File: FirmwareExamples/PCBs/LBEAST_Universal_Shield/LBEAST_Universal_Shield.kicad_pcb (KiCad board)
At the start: 2 copper layers, 118 x 84.5 mm, 54 parts, among them J1 MTJ-883X1, J10 CAN BUS, J11 FAN, J2 MTJ-883X1, J3 MTJ-883X1, J4 MTJ-883X1, J5 MTJ-883X1, J6 MTJ-883X1, J7 MTJ-883X1, J8 MTJ-883X1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

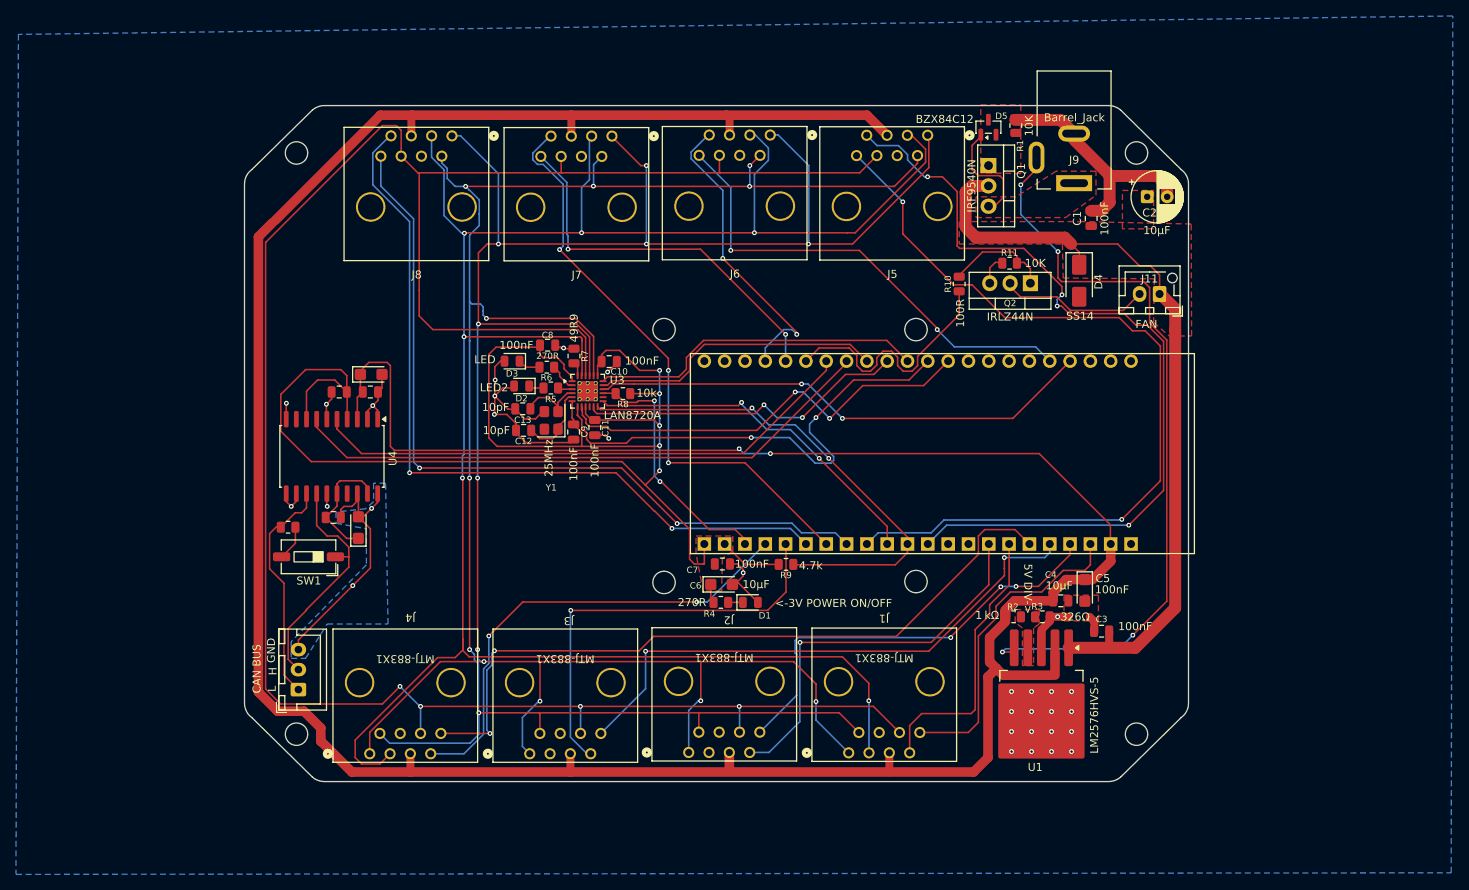
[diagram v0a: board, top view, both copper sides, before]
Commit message: add power differential protection to LBUS aux ports
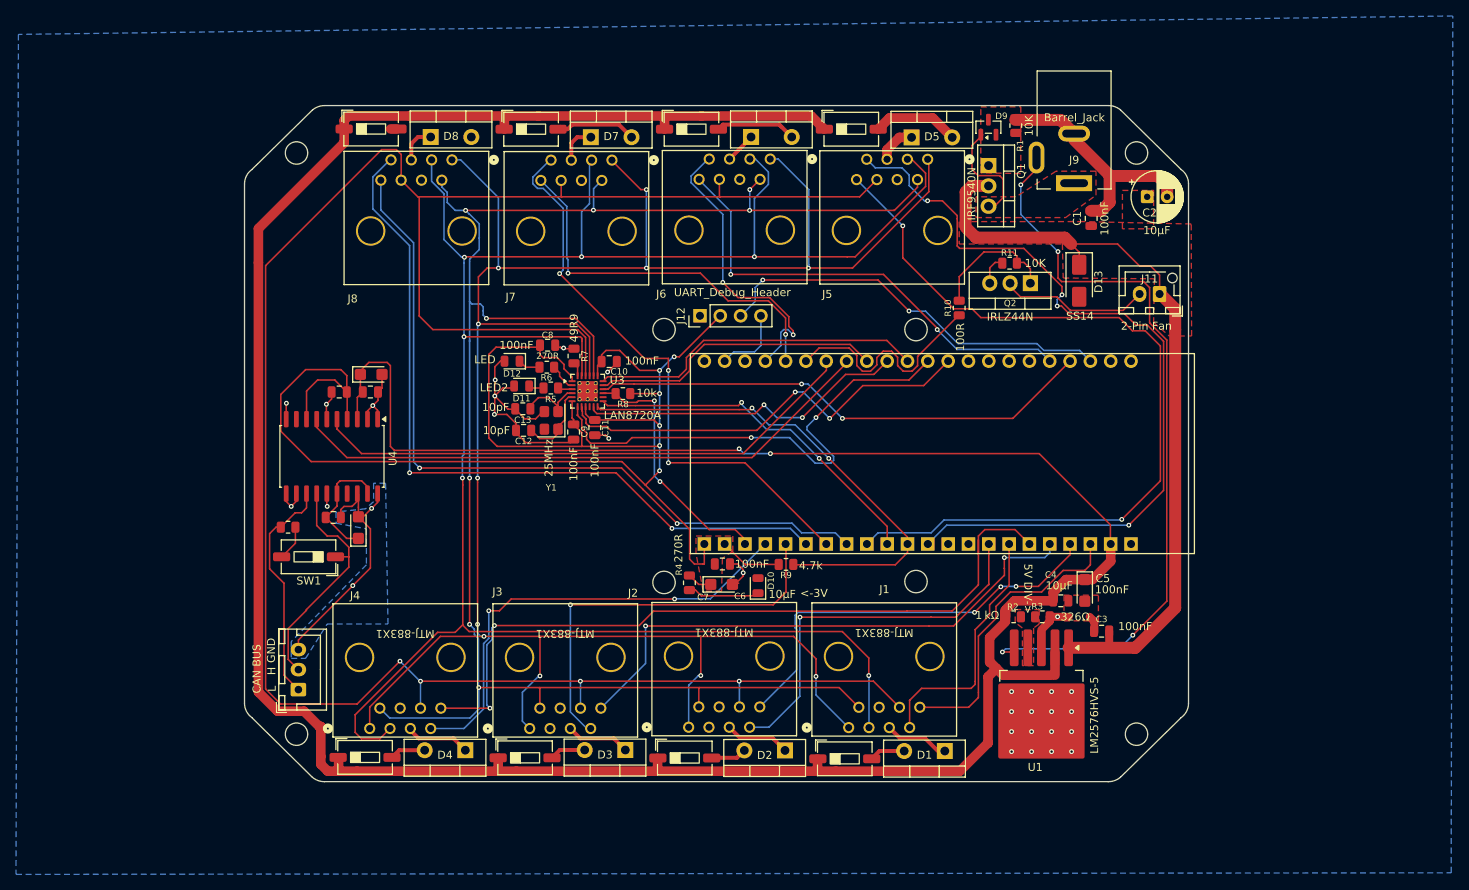
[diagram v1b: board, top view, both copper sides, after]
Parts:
- added D1: MBR735, Package_TO_SOT_THT:TO-220-2_Vertical, F.Cu at (176.1, 135.2)
- added D2: MBR735, Package_TO_SOT_THT:TO-220-2_Vertical, F.Cu at (156.1, 135.1)
- added D3: MBR735, Package_TO_SOT_THT:TO-220-2_Vertical, F.Cu at (136.2, 135.1)
- added D4: MBR735, Package_TO_SOT_THT:TO-220-2_Vertical, F.Cu at (116.2, 135.1)
- added D5: MBR735, Package_TO_SOT_THT:TO-220-2_Vertical, F.Cu at (171.9, 58.5)
- added D6: MBR735, Package_TO_SOT_THT:TO-220-2_Vertical, F.Cu at (151.9, 58.4)
- added D7: MBR735, Package_TO_SOT_THT:TO-220-2_Vertical, F.Cu at (131.9, 58.5)
- added D8: MBR735, Package_TO_SOT_THT:TO-220-2_Vertical, F.Cu at (111.8, 58.4)
- added J12: UART_Debug_Header, Connector_PinHeader_2.54mm:PinHeader_1x04_P2.54mm_Vertical, F.Cu at (145.5, 80.8)
- added SW2: J1_PWR_SW, Button_Switch_SMD:SW_DIP_SPSTx01_Slide_6.7x4.1mm_W6.73mm_P2.54mm_LowProfile_JPin, F.Cu at (163.6, 136.2)
- added SW3: J2_PWR_SW, Button_Switch_SMD:SW_DIP_SPSTx01_Slide_6.7x4.1mm_W6.73mm_P2.54mm_LowProfile_JPin, F.Cu at (143.6, 136.1)
- added SW4: J3_PWR_SW, Button_Switch_SMD:SW_DIP_SPSTx01_Slide_6.7x4.1mm_W6.73mm_P2.54mm_LowProfile_JPin, F.Cu at (123.6, 136.0)
- added SW5: J4_PWR_SW, Button_Switch_SMD:SW_DIP_SPSTx01_Slide_6.7x4.1mm_W6.73mm_P2.54mm_LowProfile_JPin, F.Cu at (103.6, 136.0)
- added SW6: J5_PWR_SW, Button_Switch_SMD:SW_DIP_SPSTx01_Slide_6.7x4.1mm_W6.73mm_P2.54mm_LowProfile_JPin, F.Cu at (164.4, 57.5)
- added SW7: J6_PWR_SW, Button_Switch_SMD:SW_DIP_SPSTx01_Slide_6.7x4.1mm_W6.73mm_P2.54mm_LowProfile_JPin, F.Cu at (144.4, 57.5)
- added SW8: J7_PWR_SW, Button_Switch_SMD:SW_DIP_SPSTx01_Slide_6.7x4.1mm_W6.73mm_P2.54mm_LowProfile_JPin, F.Cu at (124.4, 57.5)
- added SW9: J8_PWR_SW, Button_Switch_SMD:SW_DIP_SPSTx01_Slide_6.7x4.1mm_W6.73mm_P2.54mm_LowProfile_JPin, F.Cu at (104.4, 57.4)
- J11: value FAN -> 2-Pin Fan
- moved R4 4.63 mm to (144.2, 114.2), turned to -90 degrees
- moved J1 3.15 mm to (164.1, 132.2)
- moved J2 3.15 mm to (144.1, 132.2)
- moved J3 3.15 mm to (124.2, 132.4)
- moved J4 3.15 mm to (104.2, 132.4)
- moved J5 3.00 mm to (174.0, 61.2)
- moved J6 3.00 mm to (154.3, 61.2)
- moved J7 3.00 mm to (134.5, 61.3)
- moved J8 3.00 mm to (114.5, 61.3)
- moved R10 3.00 mm to (177.9, 79.8)
- moved D10 2.30 mm to (152.8, 114.5), turned to 90 degrees
- renumbered D1 to D10, D2 to D11, D3 to D12, D4 to D13, D5 to D9
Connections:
- J1 pad 5: +5V -> Net-(D1-K)
- J2 pad 5: +5V -> Net-(D2-K)
- J3 pad 5: +5V -> Net-(D3-K)
- J4 pad 5: +5V -> Net-(D4-K)
- J5 pad 5: +5V -> Net-(D5-K)
- J6 pad 5: +5V -> Net-(D6-K)
- J7 pad 5: +5V -> Net-(D7-K)
- J8 pad 5: +5V -> Net-(D8-K)
- U2 pad 24: unconnected-(U2-U0TXD-Pad24) -> /IO24
- U2 pad 42: unconnected-(U2-U0RXD-Pad42) -> /IO44
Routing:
- net /IO44: track 0.00 -> 50.8 mm, vias 0 -> 2
- net +5V: track 423.3 -> 410.8 mm
- net +3.3V: track 197.4 -> 209.0 mm, vias 5 -> 6
- net Net-(D5-A): track 0.00 -> 10.8 mm
- net Net-(D7-A): track 0.00 -> 10.5 mm
- net Net-(D6-A): track 0.00 -> 10.0 mm
- net /IO24: track 0.00 -> 9.09 mm
- net Net-(D2-K): track 0.00 -> 8.16 mm
- net Net-(D4-K): track 0.00 -> 8.16 mm
- net Net-(D1-K): track 0.00 -> 8.15 mm
- net Net-(D3-K): track 0.00 -> 8.02 mm
- net /RX+: track 267.7 -> 260.1 mm
- net Net-(D10-K): track 1.85 -> 9.01 mm
- net /TX+: track 283.1 -> 276.9 mm
- net /TX-: track 232.8 -> 226.7 mm
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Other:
- board text added: "<-3V"
- board text added: "J5"
- board text added: "J6"
- board text removed: "<-3V POWER ON/OFF"
